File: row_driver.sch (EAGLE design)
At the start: 47 parts, among them IC1 MCP23017SO, Q1 BUK98150-55A, Q2 BUK98150-55A, Q3 BUK98150-55A, Q4 BUK98150-55A, Q5 BUK98150-55A, Q6 BUK98150-55A, Q7 BUK98150-55A, Q8 BUK98150-55A, Q9 BUK98150-55A

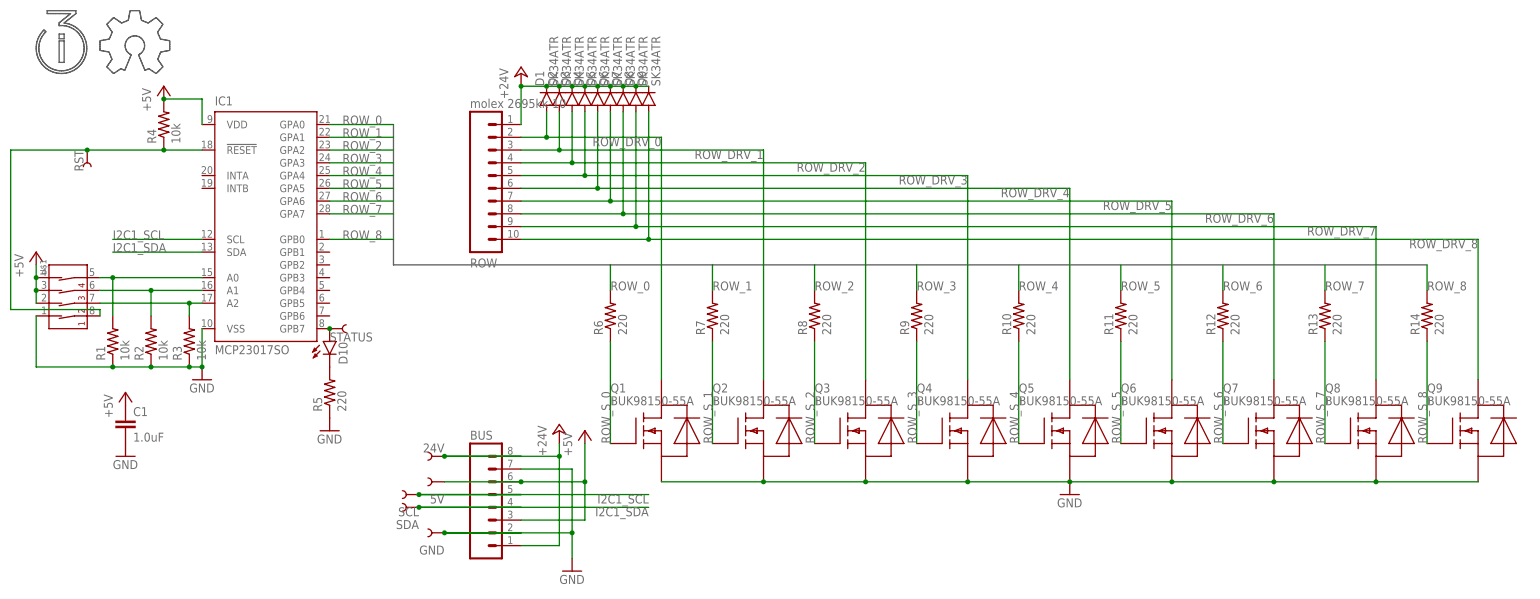
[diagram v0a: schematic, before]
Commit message: Added relay header for the ubiquitous 4-channel relay boards. Two are immediately assigned: one acts in NC in series with the compressor (so the controller can interrupt compressor power on demand, but failures restore compressor power); the other acts in NO in parallel with the bimetal thermostat (so the controller can short across it and have full compressor control, but failures allow it to function)
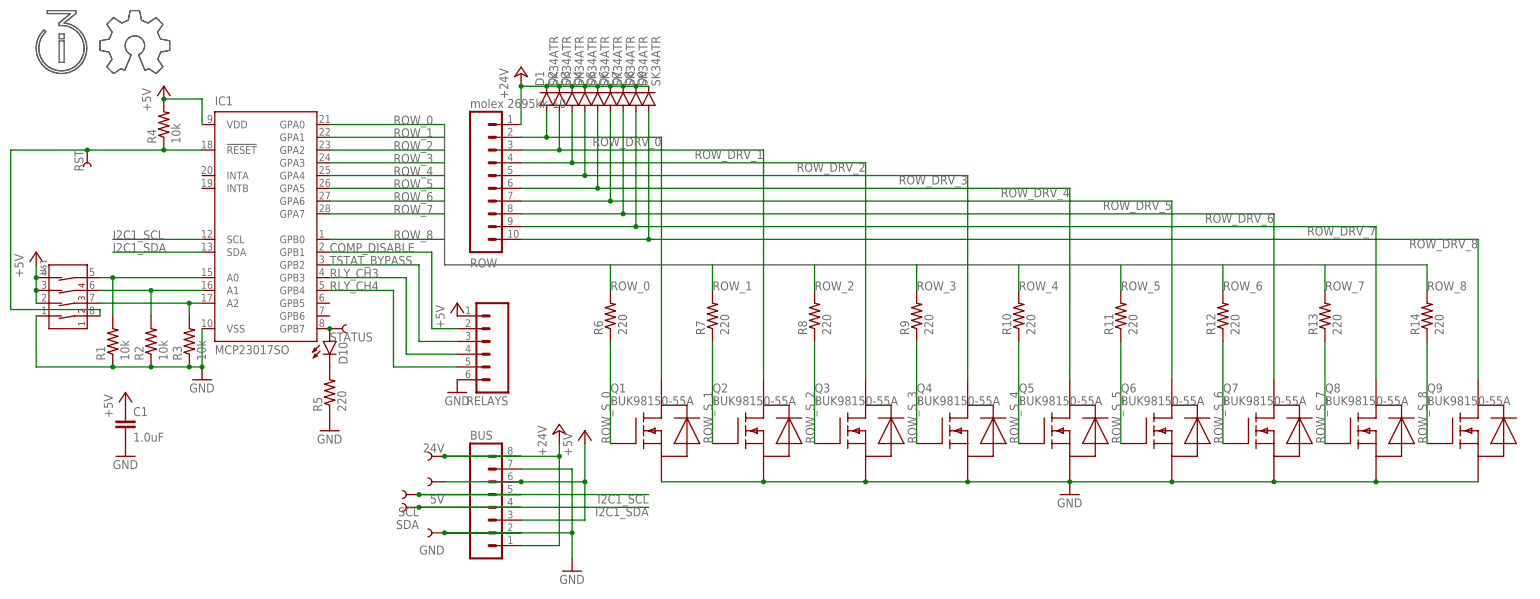
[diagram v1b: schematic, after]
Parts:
- added RELAYS: (no value), SparkFun-Connectors:M06LOCK
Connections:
- new net COMP_DISABLE: IC1.GPB1, RELAYS.2
- new net RLY_CH3: IC1.GPB3, RELAYS.4
- new net RLY_CH4: IC1.GPB4, RELAYS.5
- new net TSTAT_BYPASS: IC1.GPB2, RELAYS.3
- net +5V: now also RELAYS.1
- net GND: now also RELAYS.6
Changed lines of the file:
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@@
 <part name="R13" library="SparkFun-Passives" deviceset="RESISTOR" device="0805-RES" value="220"/>
 <part name="R14" library="SparkFun-Passives" deviceset="RESISTOR" device="0805-RES" value="220"/>
+<part name="RELAYS" library="SparkFun-Connectors" deviceset="M06" device="LOCK"/>
+<part name="GND6" library="SparkFun-Aesthetics" deviceset="GND" device=""/>
+<part name="P+6" library="supply1" deviceset="+5V" device=""/>
 </parts>
 <sheets>
@@
 <instance part="R13" gate="G$1" x="220.98" y="33.02" rot="R90"/>
 <instance part="R14" gate="G$1" x="241.3" y="33.02" rot="R90"/>
+<instance part="RELAYS" gate="G$1" x="53.34" y="27.94" rot="R180"/>
+<instance part="GND6" gate="1" x="48.26" y="17.78"/>
+<instance part="P+6" gate="1" x="48.26" y="35.56"/>
 </instances>
 <busses>
 <bus name="ROW_[0..8]">
 <segment>
-<wire x1="35.56" y1="71.12" x2="35.56" y2="43.18" width="0.762" layer="92"/>
-<wire x1="35.56" y1="43.18" x2="241.3" y2="43.18" width="0.762" layer="92"/>
+<wire x1="45.72" y1="71.12" x2="45.72" y2="43.18" width="0.762" layer="92"/>
+<wire x1="45.72" y1="43.18" x2="241.3" y2="43.18" width="0.762" layer="92"/>
 </segment>
 </bus>
@@
 <pinref part="GND5" gate="1" pin="GND"/>
 </segment>
+<segment>
+<pinref part="RELAYS" gate="G$1" pin="6"/>
+<pinref part="GND6" gate="1" pin="GND"/>
+</segment>
 </net>
 <net name="I2C1_SCL" class="0">
@@
 <segment>
 <pinref part="IC1" gate="G$1" pin="GPA0"/>
-<wire x1="35.56" y1="71.12" x2="22.86" y2="71.12" width="0.1524" layer="91"/>
-<label x="25.4" y="71.12" size="1.778" layer="95"/>
+<wire x1="45.72" y1="71.12" x2="22.86" y2="71.12" width="0.1524" layer="91"/>
+<label x="35.56" y="71.12" size="1.778" layer="95"/>
 </segment>
 <segment>
@@
 <segment>
 <pinref part="IC1" gate="G$1" pin="GPA1"/>
-<wire x1="35.56" y1="68.58" x2="22.86" y2="68.58" width="0.1524" layer="91"/>
-<label x="25.4" y="68.58" size="1.778" layer="95"/>
+<wire x1="45.72" y1="68.58" x2="22.86" y2="68.58" width="0.1524" layer="91"/>
+<label x="35.56" y="68.58" size="1.778" layer="95"/>
 </segment>
 <segment>
@@
 <segment>
 <pinref part="IC1" gate="G$1" pin="GPA2"/>
-<wire x1="35.56" y1="66.04" x2="22.86" y2="66.04" width="0.1524" layer="91"/>
-<label x="25.4" y="66.04" size="1.778" layer="95"/>
+<wire x1="45.72" y1="66.04" x2="22.86" y2="66.04" width="0.1524" layer="91"/>
+<label x="35.56" y="66.04" size="1.778" layer="95"/>
 </segment>
 <segment>
@@
 <segment>
 <pinref part="IC1" gate="G$1" pin="GPA3"/>
-<wire x1="35.56" y1="63.5" x2="22.86" y2="63.5" width="0.1524" layer="91"/>
-<label x="25.4" y="63.5" size="1.778" layer="95"/>
+<wire x1="45.72" y1="63.5" x2="22.86" y2="63.5" width="0.1524" layer="91"/>
+<label x="35.56" y="63.5" size="1.778" layer="95"/>
 </segment>
 <segment>
@@
 <segment>
 <pinref part="IC1" gate="G$1" pin="GPA4"/>
-<wire x1="35.56" y1="60.96" x2="22.86" y2="60.96" width="0.1524" layer="91"/>
-<label x="25.4" y="60.96" size="1.778" layer="95"/>
+<wire x1="45.72" y1="60.96" x2="22.86" y2="60.96" width="0.1524" layer="91"/>
+<label x="35.56" y="60.96" size="1.778" layer="95"/>
 </segment>
 <segment>
@@
 <segment>
 <pinref part="IC1" gate="G$1" pin="GPA5"/>
-<wire x1="35.56" y1="58.42" x2="22.86" y2="58.42" width="0.1524" layer="91"/>
-<label x="25.4" y="58.42" size="1.778" layer="95"/>
+<wire x1="45.72" y1="58.42" x2="22.86" y2="58.42" width="0.1524" layer="91"/>
+<label x="35.56" y="58.42" size="1.778" layer="95"/>
 </segment>
 <segment>
@@
 <segment>
 <pinref part="IC1" gate="G$1" pin="GPA6"/>
-<wire x1="35.56" y1="55.88" x2="22.86" y2="55.88" width="0.1524" layer="91"/>
-<label x="25.4" y="55.88" size="1.778" layer="95"/>
+<wire x1="45.72" y1="55.88" x2="22.86" y2="55.88" width="0.1524" layer="91"/>
+<label x="35.56" y="55.88" size="1.778" layer="95"/>
 </segment>
 <segment>
@@
 <segment>
 <pinref part="IC1" gate="G$1" pin="GPA7"/>
-<wire x1="35.56" y1="53.34" x2="22.86" y2="53.34" width="0.1524" layer="91"/>
-<label x="25.4" y="53.34" size="1.778" layer="95"/>
+<wire x1="45.72" y1="53.34" x2="22.86" y2="53.34" width="0.1524" layer="91"/>
+<label x="35.56" y="53.34" size="1.778" layer="95"/>
 </segment>
 <segment>
@@
 <segment>
 <pinref part="IC1" gate="G$1" pin="GPB0"/>
-<wire x1="35.56" y1="48.26" x2="22.86" y2="48.26" width="0.1524" layer="91"/>
-<label x="25.4" y="48.26" size="1.778" layer="95"/>
+<wire x1="45.72" y1="48.26" x2="22.86" y2="48.26" width="0.1524" layer="91"/>
+<label x="35.56" y="48.26" size="1.778" layer="95"/>
 </segment>
 <segment>
@@
 <pinref part="STATUS" gate="G$1" pin="1"/>
 <junction x="22.86" y="30.48"/>
-<pinref part="STATUS" gate="G$1" pin="1"/>
 </segment>
 </net>
@@
 <pinref part="C1" gate="G$1" pin="1"/>
 <pinref part="P+5" gate="1" pin="+5V"/>
+</segment>
+<segment>
+<pinref part="RELAYS" gate="G$1" pin="1"/>
+<pinref part="P+6" gate="1" pin="+5V"/>
 </segment>
 </net>
@@
 </segment>
 </net>
+<net name="COMP_DISABLE" class="0">
+<segment>
+<pinref part="IC1" gate="G$1" pin="GPB1"/>
+<wire x1="22.86" y1="45.72" x2="43.18" y2="45.72" width="0.1524" layer="91"/>
+<wire x1="43.18" y1="45.72" x2="43.18" y2="30.48" width="0.1524" layer="91"/>
+<pinref part="RELAYS" gate="G$1" pin="2"/>
+<wire x1="43.18" y1="30.48" x2="48.26" y2="30.48" width="0.1524" layer="91"/>
+<label x="22.86" y="45.72" size="1.778" layer="95"/>
+</segment>
+</net>
+<net name="TSTAT_BYPASS" class="0">
+<segment>
+<pinref part="IC1" gate="G$1" pin="GPB2"/>
+<wire x1="22.86" y1="43.18" x2="40.64" y2="43.18" width="0.1524" layer="91"/>
+<wire x1="40.64" y1="43.18" x2="40.64" y2="27.94" width="0.1524" layer="91"/>
+<pinref part="RELAYS" gate="G$1" pin="3"/>
+<wire x1="40.64" y1="27.94" x2="48.26" y2="27.94" width="0.1524" layer="91"/>
+<label x="22.86" y="43.18" size="1.778" layer="95"/>
+</segment>
+</net>
+<net name="RLY_CH3" class="0">
+<segment>
+<pinref part="IC1" gate="G$1" pin="GPB3"/>
+<wire x1="22.86" y1="40.64" x2="38.1" y2="40.64" width="0.1524" layer="91"/>
+<wire x1="38.1" y1="40.64" x2="38.1" y2="25.4" width="0.1524" layer="91"/>
+<pinref part="RELAYS" gate="G$1" pin="4"/>
+<wire x1="38.1" y1="25.4" x2="48.26" y2="25.4" width="0.1524" layer="91"/>
+<label x="22.86" y="40.64" size="1.778" layer="95"/>
+</segment>
+</net>
+<net name="RLY_CH4" class="0">
+<segment>
+<pinref part="IC1" gate="G$1" pin="GPB4"/>
+<wire x1="22.86" y1="38.1" x2="35.56" y2="38.1" width="0.1524" layer="91"/>
+<wire x1="35.56" y1="38.1" x2="35.56" y2="22.86" width="0.1524" layer="91"/>
+<pinref part="RELAYS" gate="G$1" pin="5"/>
+<wire x1="35.56" y1="22.86" x2="48.26" y2="22.86" width="0.1524" layer="91"/>
+<label x="22.86" y="38.1" size="1.778" layer="95"/>
+</segment>
+</net>
